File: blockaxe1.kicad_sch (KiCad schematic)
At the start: 3 parts, among them U3 RT9080-33GJ5

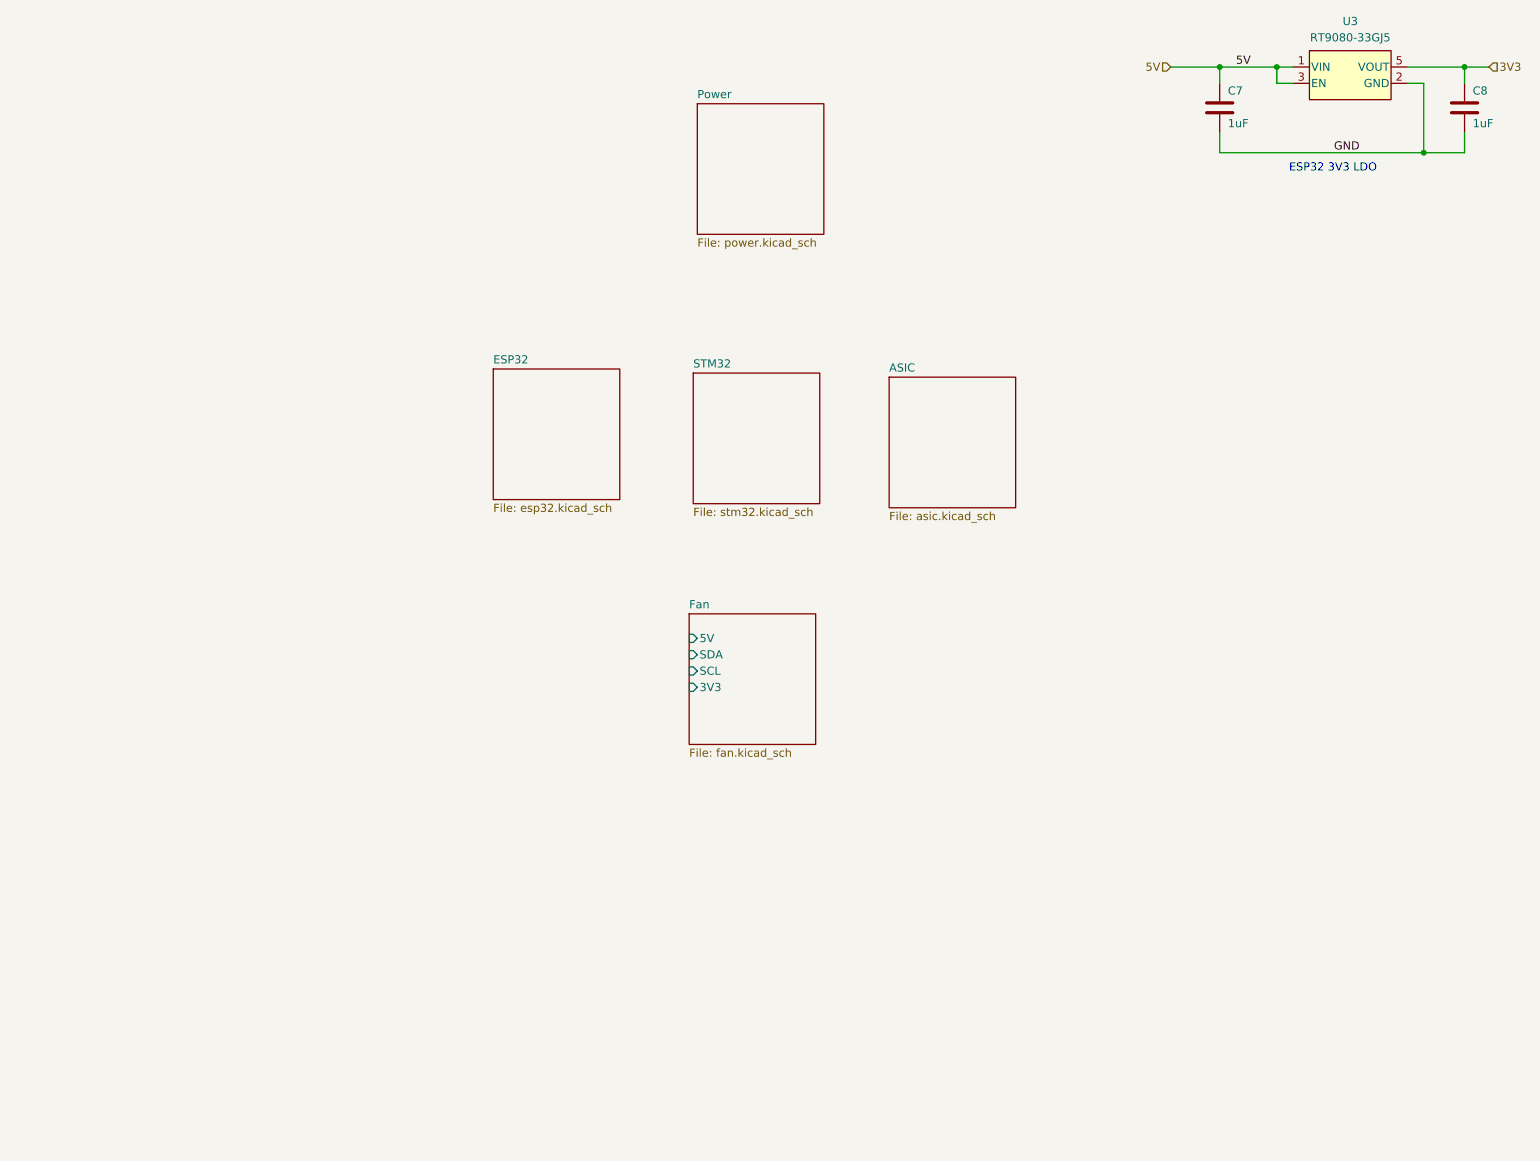
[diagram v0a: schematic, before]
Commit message: adding logo and docs
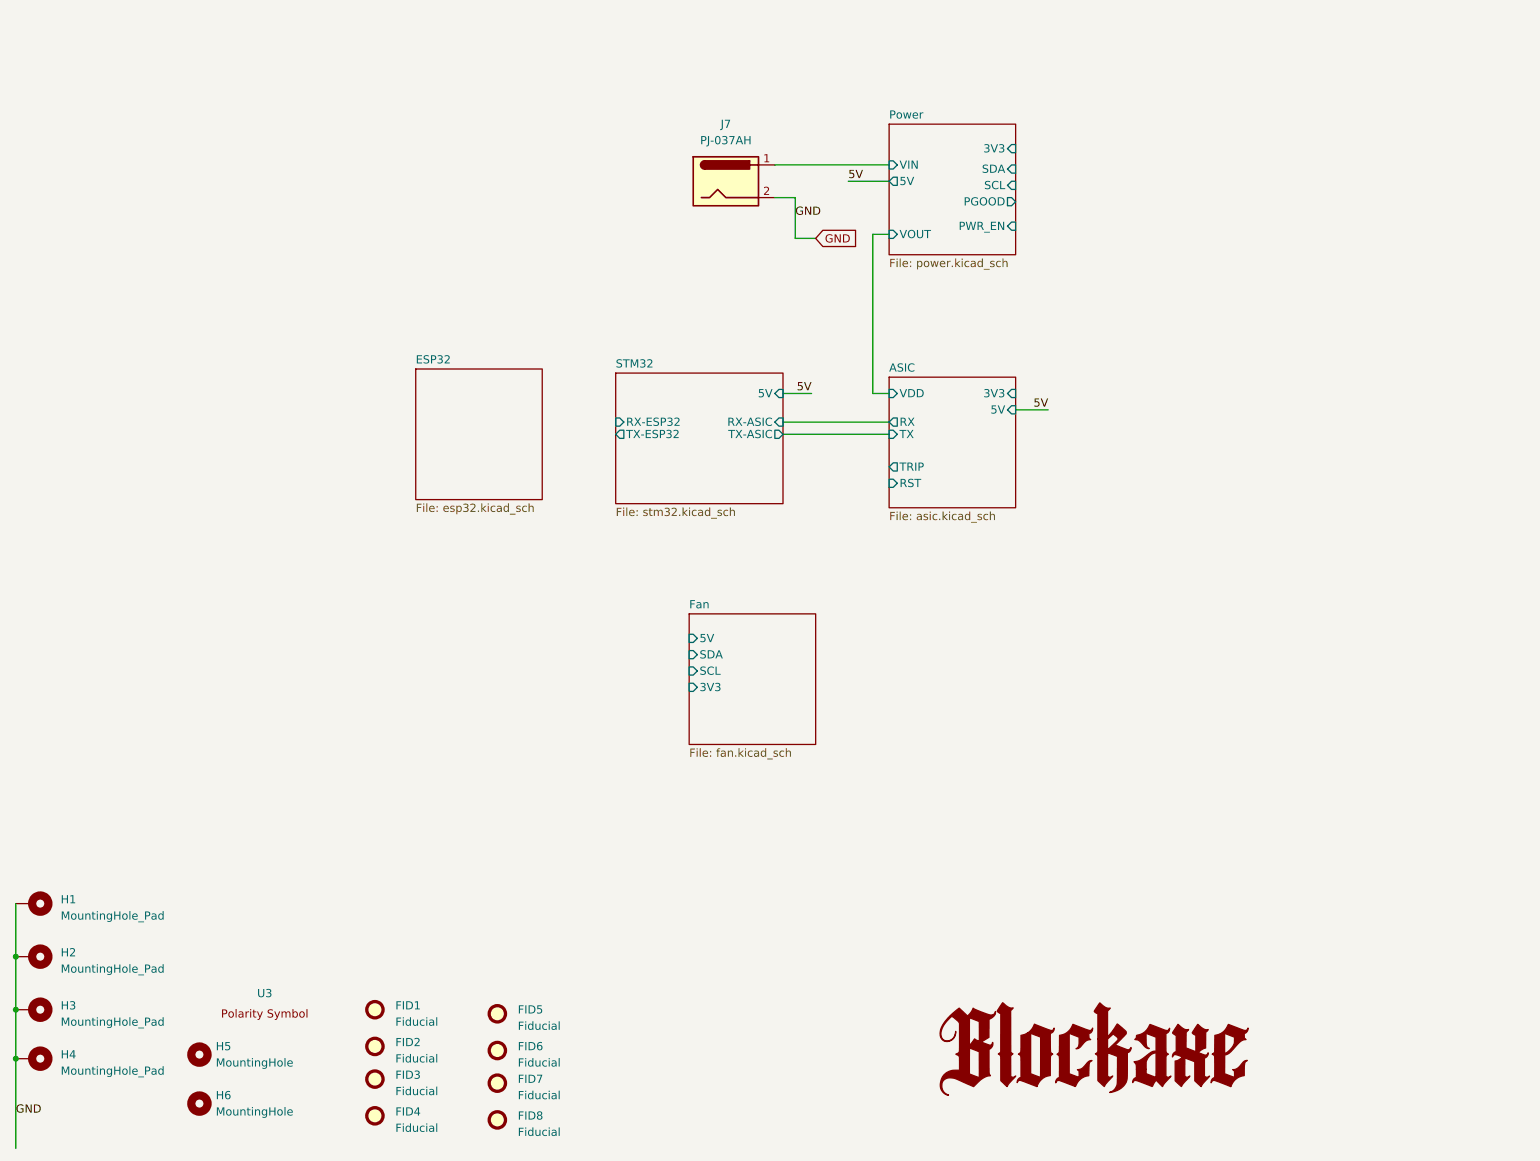
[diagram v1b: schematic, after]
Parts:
- removed C7, C8: 1uF, Capacitor_SMD:C_0402_1005Metric, symbol Device:C
- removed U3: RT9080-33GJ5, bitaxe:RT9080-33GJ5, symbol bitaxe:RT9080-33GJ5
- added FID1, FID2, FID3, FID4, FID5, FID6, FID7, FID8: Fiducial, Fiducial:Fiducial_1mm_Mask2mm, symbol Mechanical:Fiducial
- added H1, H2, H3, H4: MountingHole_Pad, MountingHole:MountingHole_3mm_Pad_Via, symbol Mechanical:MountingHole_Pad
- added H5, H6: MountingHole, MountingHole:MountingHole_3.5mm, symbol Mechanical:MountingHole
- added J7: PJ-037AH, bitaxe:CUI_PJ-037AH, symbol Connector:Barrel_Jack
- added U3: ~, bitaxe:polarity, symbol bitaxe:polarity
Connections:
- net GND: now also H1.1, H2.1, H3.1, H4.1, J7.2
- new net Power/VIN: J7.1
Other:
- sheet ASIC ports: added 3V3, 5V, RST, RX, TRIP, TX, VDD; removed none
- sheet Power ports: added 3V3, 5V, PGOOD, PWR_EN, SCL, SDA, VIN, VOUT; removed none
- sheet STM32 ports: added 5V, RX-ASIC, RX-ESP32, TX-ASIC, TX-ESP32; removed none
- note removed: "ESP32 3V3 LDO"

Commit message: added BZM2 footprint
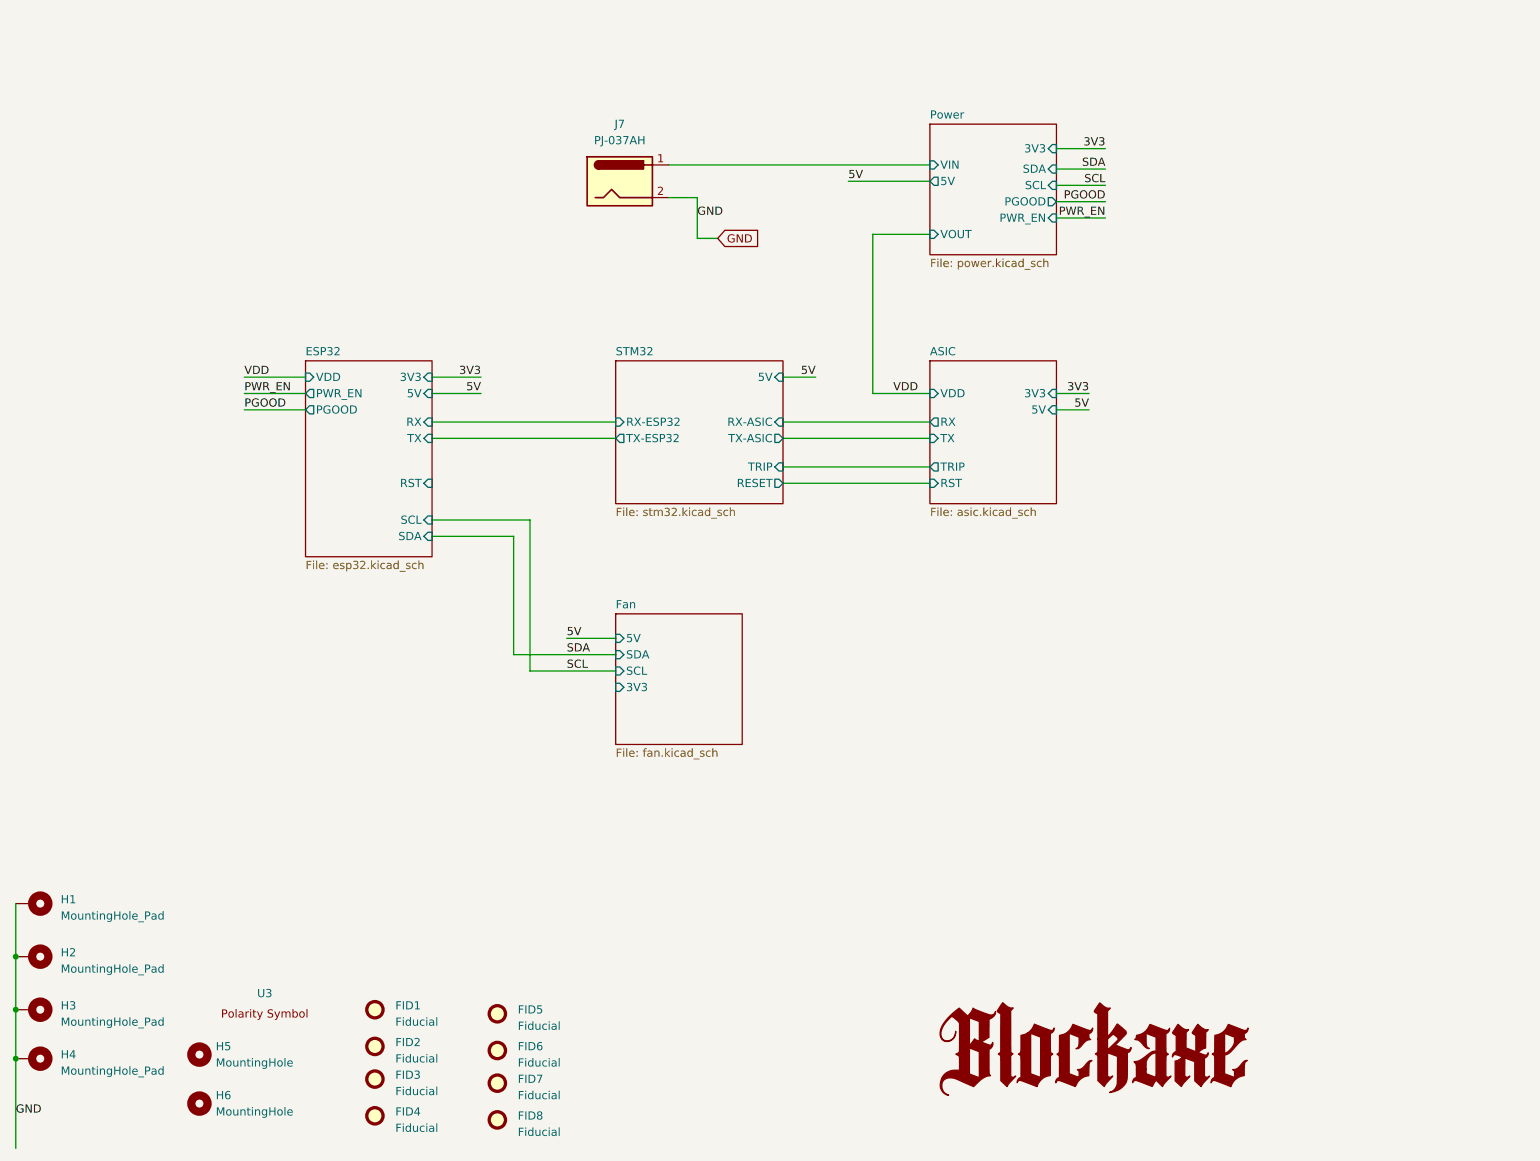
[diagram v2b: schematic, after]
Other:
- sheet ESP32 ports: added 3V3, 5V, PGOOD, PWR_EN, RST, RX, SCL, SDA, TX, VDD; removed none
- sheet STM32 ports: added RESET, TRIP; removed none
- moved on the sheet: J7

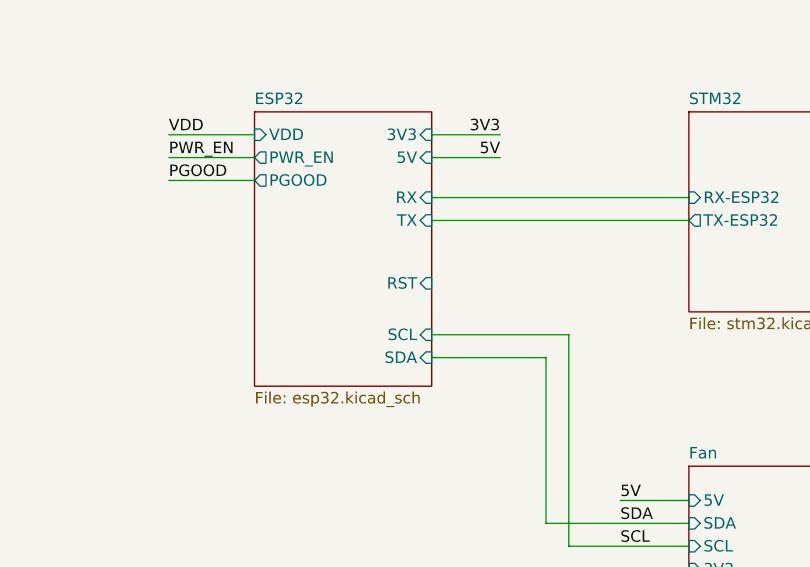
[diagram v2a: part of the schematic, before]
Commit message: migrated over lots of bitaxe parts to blockaxe
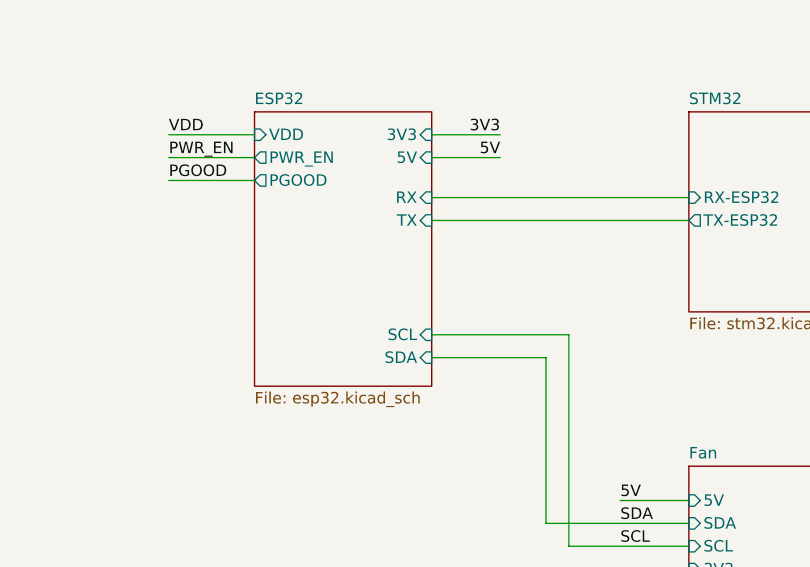
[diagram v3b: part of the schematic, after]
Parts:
- J7: footprint bitaxe:CUI_PJ-037AH -> blockaxe:CUI_PJ-037AH
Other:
- sheet ESP32 ports: added none; removed RST
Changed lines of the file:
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@@
       (effects (font (size 1.27 1.27)))
     )
-    (property "Footprint" "bitaxe:CUI_PJ-037AH" (at 130.175 39.751 0)
+    (property "Footprint" "blockaxe:CUI_PJ-037AH" (at 130.175 39.751 0)
       (effects (font (size 1.27 1.27)) hide)
     )
@@
       (effects (font (size 1.27 1.27)) (justify right))
     )
-    (pin "RST" input (at 99.695 85.725 0)
-      (effects (font (size 1.27 1.27)) (justify right))
-    )

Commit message: all the footprints are in?
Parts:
- U3: footprint bitaxe:polarity -> blockaxe:polarity
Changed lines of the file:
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@@
       (effects (font (size 1.27 1.27)))
     )
-    (property "Footprint" "bitaxe:polarity" (at 74.93 167.005 0)
+    (property "Footprint" "blockaxe:polarity" (at 74.93 167.005 0)
       (effects (font (size 1.27 1.27)) hide)
     )

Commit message: more placing and routing
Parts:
- removed J7: PJ-037AH, blockaxe:CUI_PJ-037AH, symbol Connector:Barrel_Jack
- added J5: 54-00164, blockaxe:BarrelJack_Wuerth_694106106102_2.0x5.5mm, symbol Connector:Barrel_Jack_Switch
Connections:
- net GND: now also J5.2
- net Power/VIN: now also J5.1
- new net PLUG_SENSE: J5.3
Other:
- sheet ASIC ports: added none; removed 5V

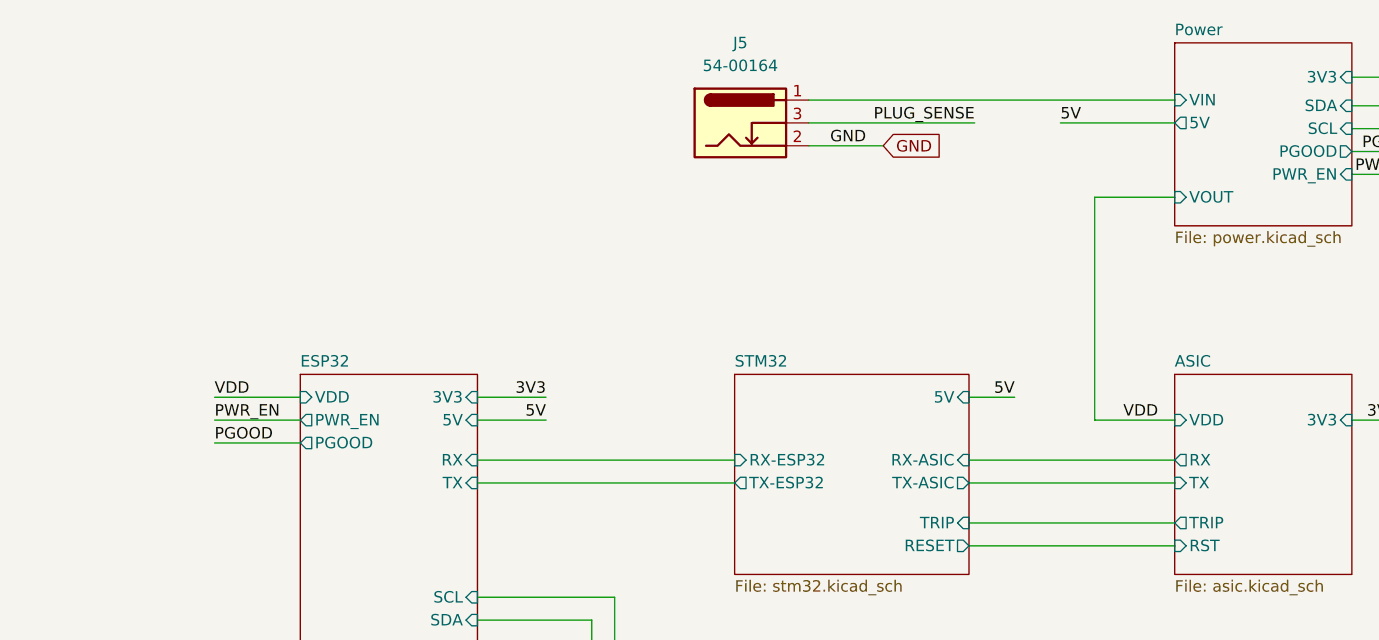
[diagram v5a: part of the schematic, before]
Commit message: more routing. switched to RA buttons, moved the buck closer to the barrel
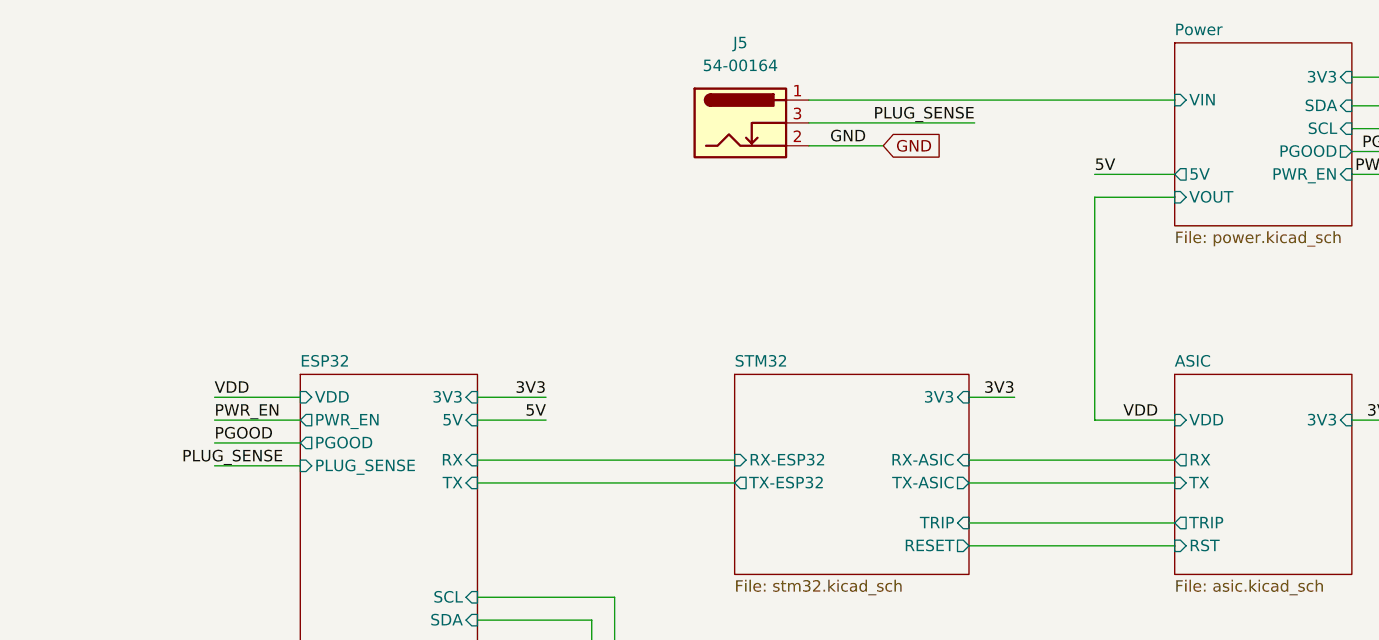
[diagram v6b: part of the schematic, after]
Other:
- sheet ESP32 ports: added PLUG_SENSE; removed none
- sheet STM32 ports: added 3V3; removed 5V
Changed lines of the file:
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@@
-    (stroke (width 0) (type default))
-  )
-  (wire (pts (xy 164.465 38.735) (xy 177.165 38.735))
     (stroke (width 0) (type default))
   )
@@
     (stroke (width 0) (type default))
   )
+  (wire (pts (xy 168.275 44.45) (xy 177.165 44.45))
+    (stroke (width 0) (type default))
+  )
   (wire (pts (xy 154.305 83.185) (xy 177.165 83.185))
     (stroke (width 0) (type default))
@@
     (stroke (width 0) (type default))
   )
+  (wire (pts (xy 70.485 76.835) (xy 80.01 76.835))
+    (stroke (width 0) (type default))
+  )
   (wire (pts (xy 154.305 76.2) (xy 177.165 76.2))
     (stroke (width 0) (type default))
@@
     (effects (font (size 1.27 1.27)) (justify right bottom))
   )
-  (label "5V" (at 159.385 69.215 180) (fields_autoplaced)
+  (label "3V3" (at 159.385 69.215 180) (fields_autoplaced)
+    (effects (font (size 1.27 1.27)) (justify right bottom))
+  )
+  (label "PLUG_SENSE" (at 78.105 76.835 180) (fields_autoplaced)
     (effects (font (size 1.27 1.27)) (justify right bottom))
   )
@@
     (effects (font (size 1.27 1.27)) (justify right bottom))
   )
-  (label "5V" (at 164.465 38.735 0) (fields_autoplaced)
+  (label "5V" (at 168.275 44.45 0) (fields_autoplaced)
     (effects (font (size 1.27 1.27)) (justify left bottom))
   )
@@
       (effects (font (size 1.27 1.27)) (justify right))
     )
+    (pin "PLUG_SENSE" input (at 80.01 76.835 180)
+      (effects (font (size 1.27 1.27)) (justify left))
+    )
     (instances
       (project "blockaxe1"
@@
       (effects (font (size 1.27 1.27)) (justify right))
     )
-    (pin "5V" input (at 154.305 69.215 0)
-      (effects (font (size 1.27 1.27)) (justify right))
-    )
     (pin "TRIP" input (at 154.305 83.185 0)
       (effects (font (size 1.27 1.27)) (justify right))
     )
     (pin "RESET" output (at 154.305 85.725 0)
+      (effects (font (size 1.27 1.27)) (justify right))
+    )
+    (pin "3V3" input (at 154.305 69.215 0)
       (effects (font (size 1.27 1.27)) (justify right))
     )
@@
       (effects (font (size 1.27 1.27)) (justify right))
     )
-    (pin "5V" output (at 177.165 38.735 180)
-      (effects (font (size 1.27 1.27)) (justify left))
-    )
+    (pin "5V" output (at 177.165 44.45 180)
+      (effects (font (size 1.27 1.27)) (justify left))
+    )
